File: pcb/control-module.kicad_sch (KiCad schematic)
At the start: 27 parts, among them J1 Screw_Terminal_01x06, J2 Conn_01x07_Pin, SW1 SW_DIP_x04, U1 TC2185-3.3VxCTTR

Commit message: Updated Schematics
Completed Schematics for Test Bed, updated pcb
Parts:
- removed C1, C3: 1uF, Capacitor_SMD:C_0603_1608Metric, symbol Device:C
- removed C2: 0.01uF, Capacitor_SMD:C_0603_1608Metric, symbol Device:C
- removed TP_3V3_reg: TestPoint, TestPoint:TestPoint_Loop_D2.54mm_Drill1.5mm_Beaded, symbol Connector:TestPoint
- removed U1: TC2185-3.3VxCTTR, Package_TO_SOT_SMD:SOT-23-5, symbol Regulator_Linear:TC2185-3.3VxCTTR
- added R1: 300k, Resistor_SMD:R_0603_1608Metric_Pad0.98x0.95mm_HandSolder, symbol Device:R_US
- added R2: 100k, Resistor_SMD:R_0603_1608Metric_Pad0.98x0.95mm_HandSolder, symbol Device:R_US
- added R4: 10k, Resistor_SMD:R_0603_1608Metric, symbol Device:R_US
- added TP_Power_Mux_STAT1, TP_V_{BAT}1, TP_V_{mux}1: TestPoint, TestPoint:TestPoint_Loop_D2.54mm_Drill1.5mm_Beaded, symbol Connector:TestPoint
- added U1: TPS2116DRL, Package_TO_SOT_SMD:SOT-583-8, symbol Power_Management:TPS2116DRL
- renumbered R2 to R3, R3 to R5, TP_BATT to TP_BATT1, TP_BAT_SENSE_MID to TP_BAT_SENSE_MID1
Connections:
- net +3.3V: now also R4.1
- net GNDD: now also R2.1, U1.1 (GND)
- net V_USB: now also R1.2, U1.3 (VIN1), U1.5 (MODE)
- new net: R1.1, R2.2, U1.4 (PR1)
- new net: R4.2, TP_Power_Mux_STAT1.1, U1.8 (ST)
- new net Battery/V_{BAT}: TP_V_{BAT}1.1
- new net Battery/V_{mux}: TP_V_{mux}1.1
- new net V_{BAT}: U1.6 (VIN2)
- new net V_{mux}: U1.2 (VOUT), U1.7 (VOUT)
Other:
- sheet Battery ports: added V_{BAT}, V_{mux}; removed none
- note removed: "USB Voltage Regulator"
- moved on the sheet: D1, D2, FID1, FID2, FID3, R3, R5

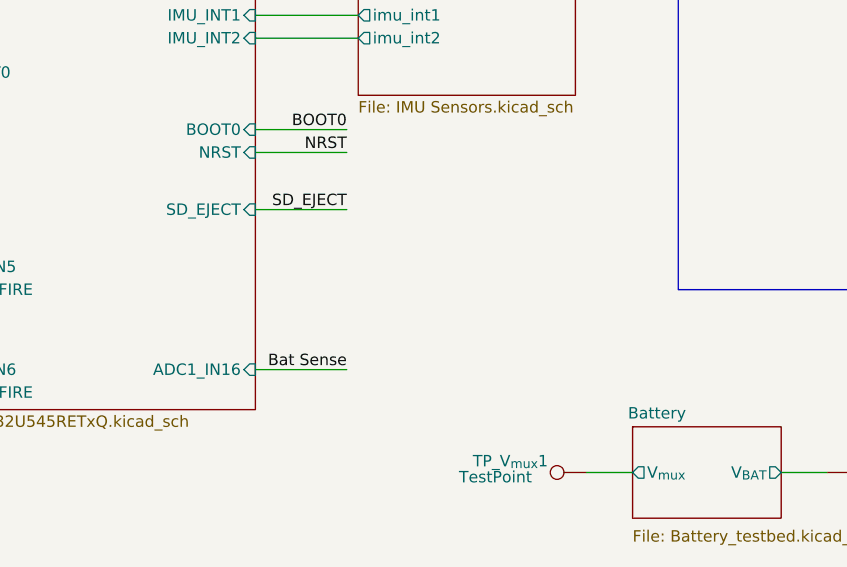
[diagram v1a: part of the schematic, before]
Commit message: Completed most of testbed layout
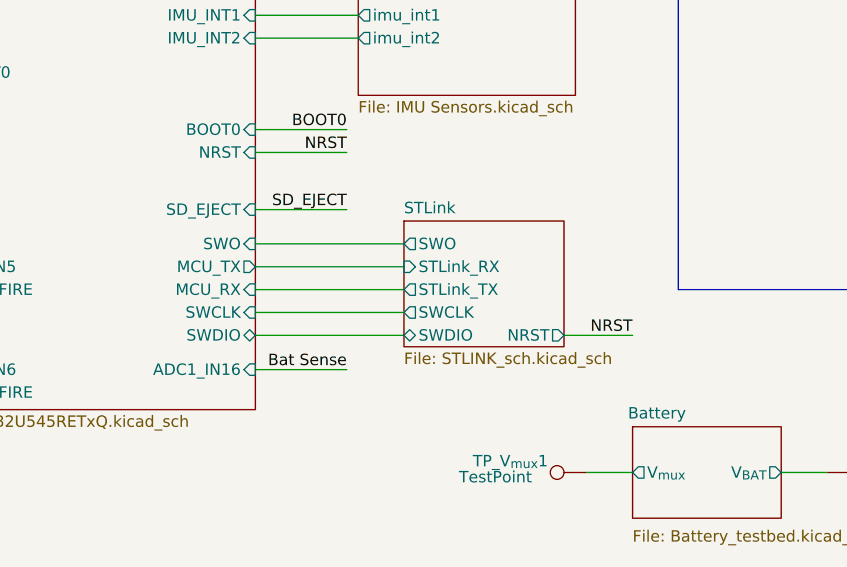
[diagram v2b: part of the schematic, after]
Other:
- added sheet STLink (STLINK_sch.kicad_sch)
- sheet MCU ports: added MCU_RX, MCU_TX, SWCLK, SWDIO, SWO; removed none
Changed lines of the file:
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@@
 	(wire
 		(pts
+			(xy 142.24 127) (xy 158.75 127)
+		)
+		(stroke
+			(width 0)
+			(type default)
+		)
+	)
+	(wire
+		(pts
 			(xy 67.31 133.35) (xy 41.91 133.35)
 		)
@@
 	(wire
 		(pts
+			(xy 142.24 129.54) (xy 158.75 129.54)
+		)
+		(stroke
+			(width 0)
+			(type default)
+		)
+	)
+	(wire
+		(pts
 			(xy 80.01 153.67) (xy 83.82 153.67)
 		)
@@
 	(wire
 		(pts
+			(xy 142.24 124.46) (xy 158.75 124.46)
+		)
+		(stroke
+			(width 0)
+			(type default)
+		)
+	)
+	(wire
+		(pts
 			(xy 93.98 129.54) (xy 105.41 129.54)
 		)
@@
 	(wire
 		(pts
+			(xy 142.24 134.62) (xy 158.75 134.62)
+		)
+		(stroke
+			(width 0)
+			(type default)
+		)
+	)
+	(wire
+		(pts
 			(xy 115.57 173.99) (xy 113.03 173.99)
 		)
@@
 	(wire
 		(pts
+			(xy 142.24 132.08) (xy 158.75 132.08)
+		)
+		(stroke
+			(width 0)
+			(type default)
+		)
+	)
+	(wire
+		(pts
 			(xy 83.82 165.1) (xy 90.17 165.1)
 		)
@@
 	(wire
 		(pts
+			(xy 176.53 134.62) (xy 184.15 134.62)
+		)
+		(stroke
+			(width 0)
+			(type default)
+		)
+	)
+	(wire
+		(pts
 			(xy 91.44 22.86) (xy 99.06 22.86)
 		)
@@
 		)
 	)
+	(label "NRST"
+		(at 184.15 134.62 180)
+		(effects
+			(font
+				(size 1.27 1.27)
+			)
+			(justify right bottom)
+		)
+	)
 	(label "V_USB"
 		(at 76.2 153.67 180)
@@
 			)
 		)
+		(pin "MCU_TX" output
+			(at 142.24 127 0)
+			(effects
+				(font
+					(size 1.27 1.27)
+				)
+				(justify right)
+			)
+		)
+		(pin "MCU_RX" input
+			(at 142.24 129.54 0)
+			(effects
+				(font
+					(size 1.27 1.27)
+				)
+				(justify right)
+			)
+		)
+		(pin "SWCLK" input
+			(at 142.24 132.08 0)
+			(effects
+				(font
+					(size 1.27 1.27)
+				)
+				(justify right)
+			)
+		)
+		(pin "SWDIO" bidirectional
+			(at 142.24 134.62 0)
+			(effects
+				(font
+					(size 1.27 1.27)
+				)
+				(justify right)
+			)
+		)
+		(pin "SWO" input
+			(at 142.24 124.46 0)
+			(effects
+				(font
+					(size 1.27 1.27)
+				)
+				(justify right)
+			)
+		)
 		(instances
 			(project "control-module"
@@
 				)
 			)
+		)
+	)
+	(sheet
+		(at 158.75 121.92)
+		(size 17.78 13.97)
+		(exclude_from_sim no)
+		(in_bom yes)
+		(on_board yes)
+		(dnp no)
+		(fields_autoplaced yes)
+		(stroke
+			(width 0.1524)
+			(type solid)
+		)
+		(fill
+			(color 0 0 0 0.0000)
+		)
+		(property "Sheetname" "STLink"
+			(at 158.75 121.2084 0)
+			(effects
+				(font
+					(size 1.27 1.27)
+				)
+				(justify left bottom)
+			)
+		)
+		(property "Sheetfile" "STLINK_sch.kicad_sch"
+			(at 158.75 136.4746 0)
+			(effects
+				(font
+					(size 1.27 1.27)
+				)
+				(justify left top)
+			)
+		)
+		(pin "NRST" output
+			(at 176.53 134.62 0)
+			(effects
+				(font
+					(size 1.27 1.27)
+				)
+				(justify right)
+			)
+		)
+		(pin "STLink_RX" input
+			(at 158.75 127 180)
+			(effects
+				(font
+					(size 1.27 1.27)
+				)
+				(justify left)
+			)
+		)
+		(pin "STLink_TX" output
+			(at 158.75 129.54 180)
+			(effects
+				(font
+					(size 1.27 1.27)
+				)
+				(justify left)
+			)
+		)
+		(pin "SWCLK" output
+			(at 158.75 132.08 180)
+			(effects
+				(font
+					(size 1.27 1.27)
+				)
+				(justify left)
+			)
+		)
+		(pin "SWDIO" bidirectional
+			(at 158.75 134.62 180)
+			(effects
+				(font
+					(size 1.27 1.27)
+				)
+				(justify left)
+			)
+		)
+		(pin "SWO" output
+			(at 158.75 124.46 180)
+			(effects
+				(font
+					(size 1.27 1.27)
+				)
+				(justify left)
+			)
+		)
+		(instances
+			(project "control-module"
+				(path "/ba7b4294-8d75-4b9e-892f-fb52727887ec"
+					(page "9")
+				)
+			)
